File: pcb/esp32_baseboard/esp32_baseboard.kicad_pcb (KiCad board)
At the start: 2 copper layers, 220 x 160 mm, 49 parts, among them J1 Screw_12V_IN, J10 END_HOME2, J12 END_HOME3, J14 BUP_30S, J15 BUZZER_5V, J16 AOD4184, J17 TFT_LCD, J18 EC11_ENC, J23 TFT_TP, J24 595_CTRL, J25 595_Q, J5 28BYJ48, J6 28BYJ48, J7 28BYJ48, J8 END_HOME1, U1 ESP32_S3_DevKitC_1, U2 MP1584_5V3A, U3 TMC2209, U41 PC817, U42 PC817, U43 PC817, U44 PC817, U5 ULN2003AN, U6 ULN2003AN, U7 ULN2003AN

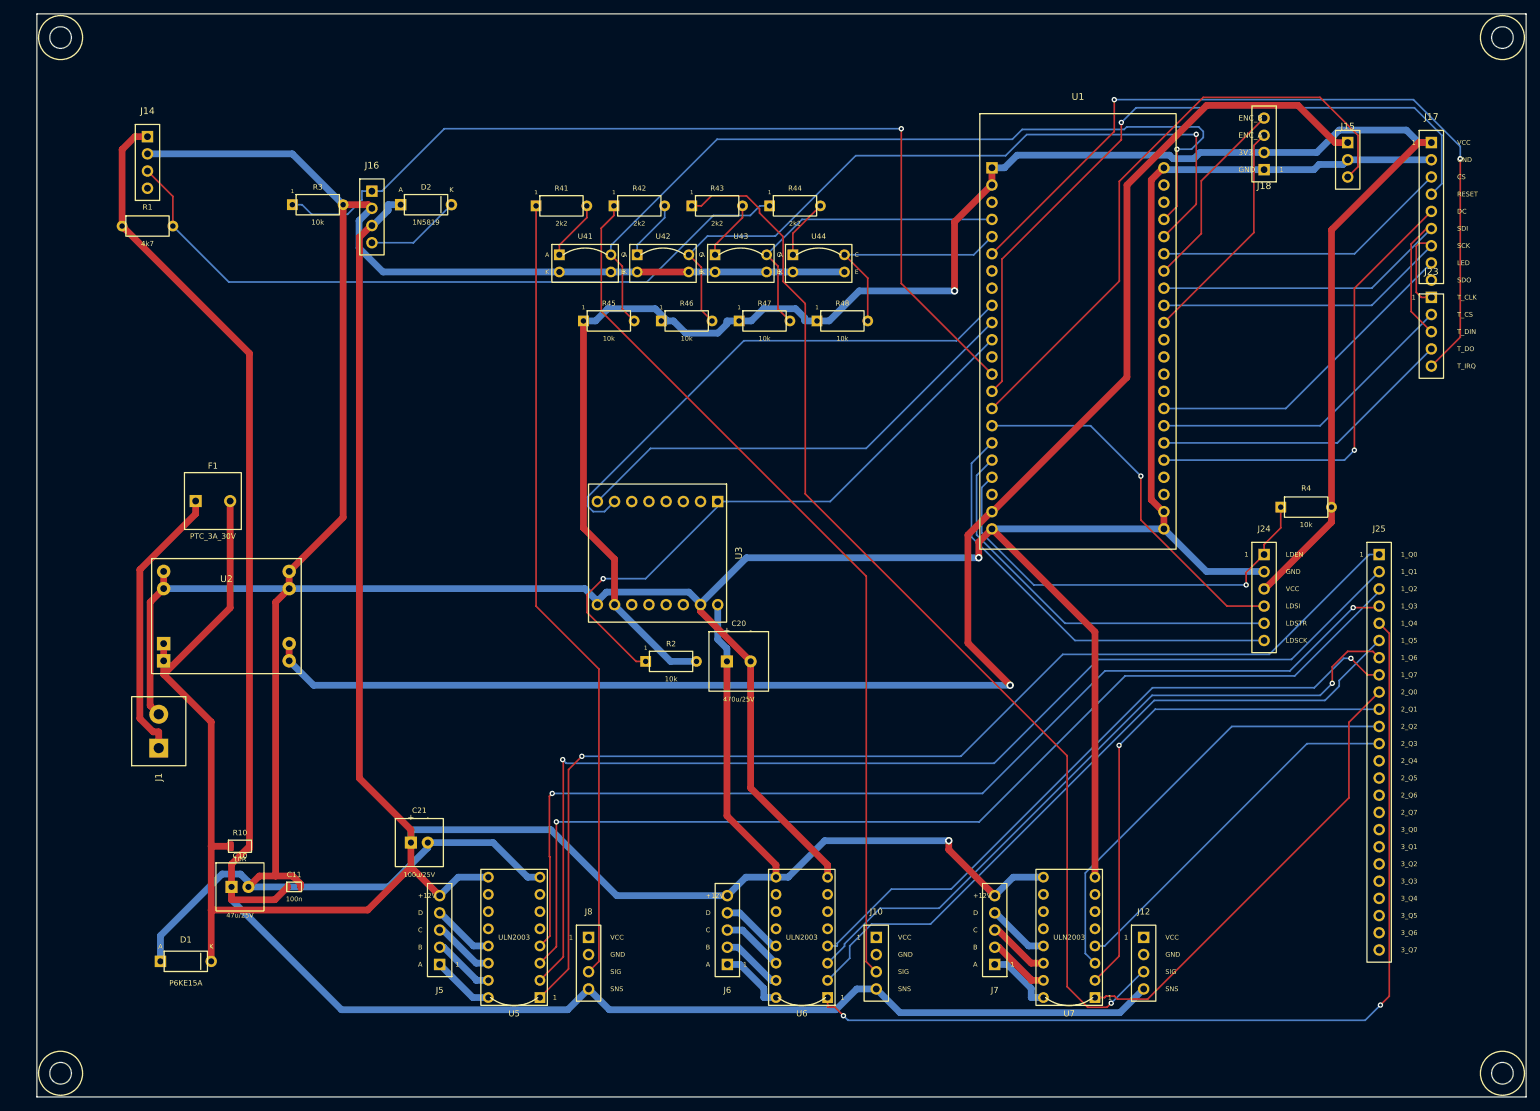
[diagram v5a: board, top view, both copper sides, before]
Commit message: update PCB cho phần power và opto và sắp xếp linh kiện
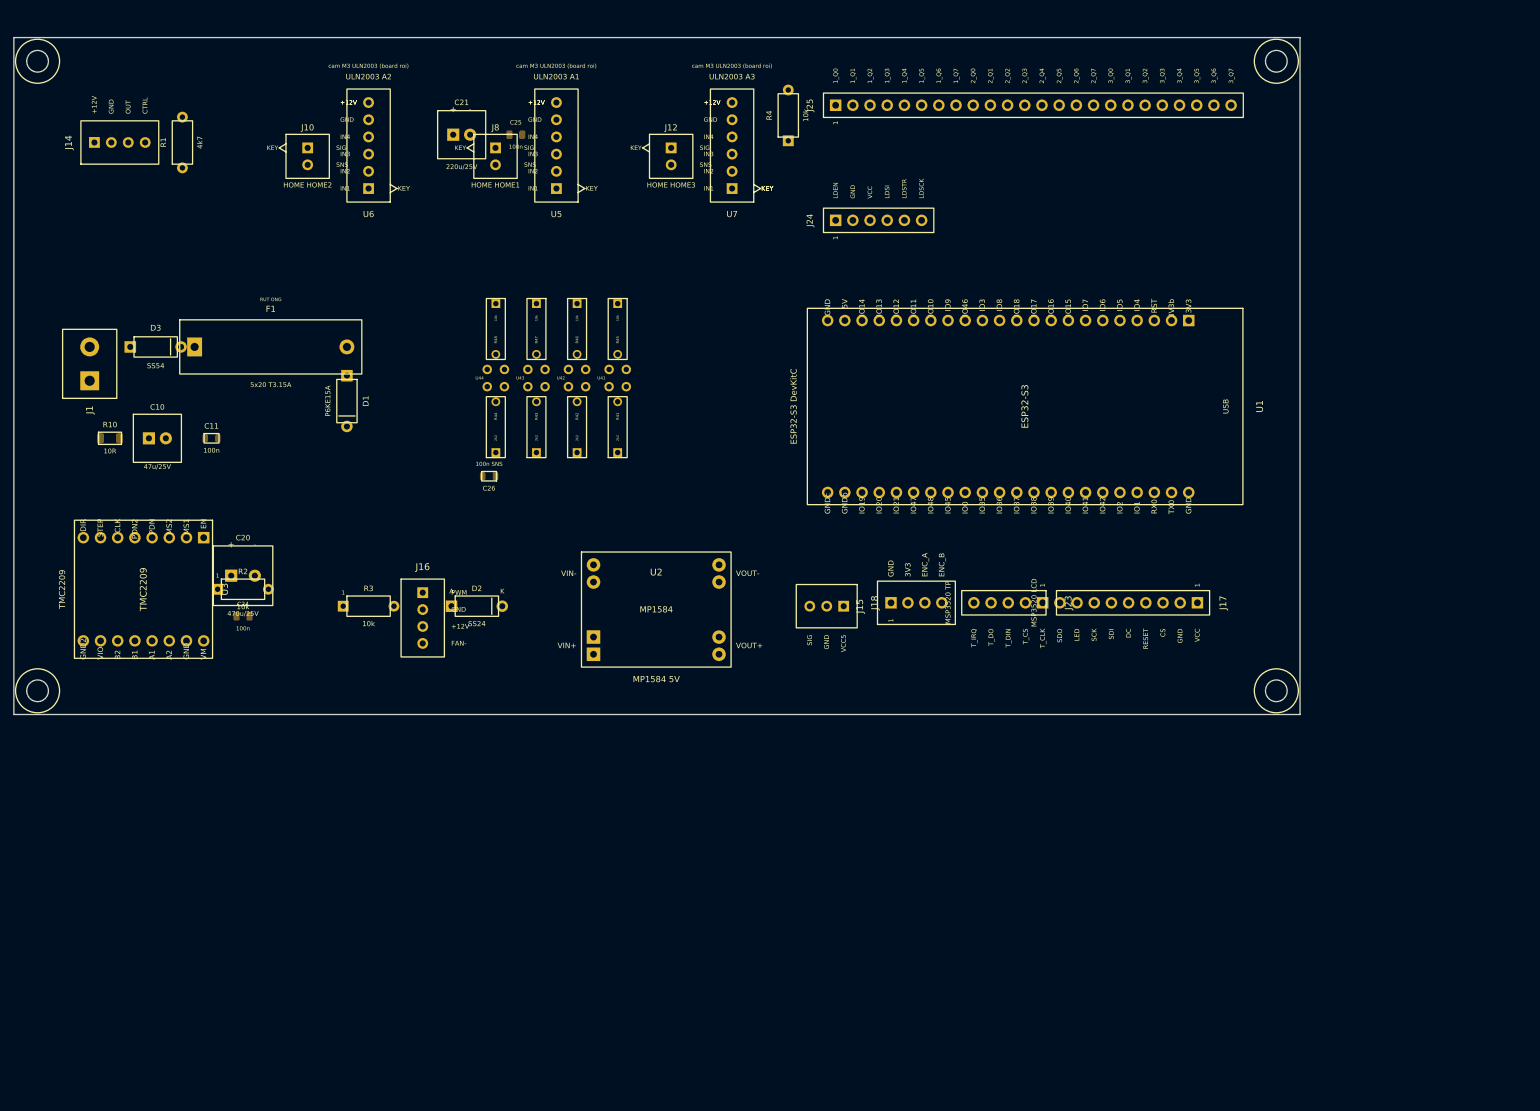
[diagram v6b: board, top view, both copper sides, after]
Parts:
- removed J5, J6, J7: 28BYJ48, ESP32_Carrier:PinHeader_1x05_BYJ
- added C24: 100n, ESP32_Carrier:C_0805_100n, F.Cu at (65.5, 119.0)
- added C25: 100n, ESP32_Carrier:C_0805_100n, F.Cu at (105.8, 47.9)
- added C26: 100n SNS, ESP32_Carrier:C_0805_100n, F.Cu at (101.8, 98.3)
- added D3: SS54, ESP32_Carrier:Diode_TVS_DO41, F.Cu at (52.5, 79.2)
- C21: value 100u/25V -> 220u/25V
- D2: value 1N5819 -> SS24
- F1: value PTC_3A_30V -> 5x20 T3.15A; footprint ESP32_Carrier:Fuse_PTC_Radial_5.1mm -> ESP32_Carrier:Fuse_Holder_5x20_Open
- J10: value END_HOME2 -> HOME HOME2; footprint ESP32_Carrier:PinHeader_1x04_Endstop -> ESP32_Carrier:JST_XH_02_Socket
- J12: value END_HOME3 -> HOME HOME3; footprint ESP32_Carrier:PinHeader_1x04_Endstop -> ESP32_Carrier:JST_XH_02_Socket
- J14: value BUP_30S -> BUP-30S; footprint ESP32_Carrier:PinHeader_1x04_BUP30S -> ESP32_Carrier:JST_XH_04_Socket
- J15: value BUZZER_5V -> BUZZER 5V; footprint ESP32_Carrier:PinHeader_1x03_Buzzer -> ESP32_Carrier:JST_XH_03_Socket
- J16: value AOD4184 -> AOD4184 12V; footprint ESP32_Carrier:PinHeader_1x04_MOSFET -> ESP32_Carrier:JST_XH_04_Socket
- J17: value TFT_LCD -> MSP3520 LCD
- J18: value EC11_ENC -> EC11 ENC; footprint ESP32_Carrier:PinHeader_1x04_ENC -> ESP32_Carrier:JST_XH_04_Socket
- J23: value TFT_TP -> MSP3520 TP
- J8: value END_HOME1 -> HOME HOME1; footprint ESP32_Carrier:PinHeader_1x04_Endstop -> ESP32_Carrier:JST_XH_02_Socket
- U1: value ESP32_S3_DevKitC_1 -> ESP32-S3 DevKitC
- U2: value MP1584_5V3A -> MP1584 5V
- U5: value ULN2003AN -> ULN2003 A1; footprint ESP32_Carrier:ULN2003AN -> ESP32_Carrier:ULN2003_Module
- U6: value ULN2003AN -> ULN2003 A2; footprint ESP32_Carrier:ULN2003AN -> ESP32_Carrier:ULN2003_Module
- U7: value ULN2003AN -> ULN2003 A3; footprint ESP32_Carrier:ULN2003AN -> ESP32_Carrier:ULN2003_Module
- moved J10 143.7 mm to (75.0, 49.8)
- moved J12 135.9 mm to (128.7, 49.8)
- moved U6 127.8 mm to (84.0, 55.8)
- moved U7 121.3 mm to (137.7, 55.8)
- moved J8 117.4 mm to (102.8, 49.8)
- moved U5 110.8 mm to (111.8, 55.8)
- moved C21 104.8 mm to (97.8, 47.9)
- moved J25 104.2 mm to (153.0, 43.5), turned to 90 degrees
- moved J15 101.2 mm to (154.2, 117.5), turned to -90 degrees
- moved R4 95.9 mm to (146.0, 45.0), turned to 90 degrees
- moved D1 86.1 mm to (80.8, 87.2), turned to -90 degrees
- moved J18 84.4 mm to (161.2, 117.0), turned to 90 degrees
- moved J24 80.3 mm to (153.0, 60.5), turned to 90 degrees
- moved J17 76.3 mm to (206.4, 117.0), turned to -90 degrees
- moved U3 76.1 mm to (50.8, 115.0)
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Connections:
- F1 pad 1: +12V_RAW -> +12V_PRE
- J10 pad 1: unconnected-(J10-VCC-Pad1) -> OPTO_IN2
- J10 pad 2: unconnected-(J10-GND-Pad2) -> +12V_SNS
- J12 pad 1: unconnected-(J12-VCC-Pad1) -> OPTO_IN3
- J12 pad 2: unconnected-(J12-GND-Pad2) -> +12V_SNS
- J8 pad 1: unconnected-(J8-VCC-Pad1) -> OPTO_IN1
- J8 pad 2: unconnected-(J8-GND-Pad2) -> +12V_SNS
- U5 pad 5: unconnected-(U5-IN5-Pad5) -> GND
- U5 pad 6: unconnected-(U5-IN6-Pad6) -> +12V
- U6 pad 5: unconnected-(U6-IN5-Pad5) -> GND
- U6 pad 6: unconnected-(U6-IN6-Pad6) -> +12V
- U7 pad 5: unconnected-(U7-IN5-Pad5) -> GND
- U7 pad 6: unconnected-(U7-IN6-Pad6) -> +12V
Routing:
- net GND: track 696.4 -> 0.00 mm, vias 1 -> 0
- net +12V: track 385.4 -> 0.00 mm, vias 1 -> 0
- net +3V3: track 288.3 -> 0.00 mm, vias 1 -> 0
- net +12V_SNS: track 283.4 -> 0.00 mm
- net +5V: track 236.6 -> 0.00 mm, vias 1 -> 0
- net SR_Q0: track 168.3 -> 0.00 mm, vias 1 -> 0
- net SR_Q1: track 166.6 -> 0.00 mm, vias 1 -> 0
- net OPTO_IN3: track 159.9 -> 0.00 mm, vias 1 -> 0
- net SR_Q2: track 157.9 -> 0.00 mm, vias 1 -> 0
- net SR_Q3: track 157.0 -> 0.00 mm, vias 2 -> 0
- net SR_Q4: track 142.4 -> 0.00 mm, vias 2 -> 0
- net BLOWER: track 138.3 -> 0.00 mm, vias 1 -> 0
- net OPTO_IN2: track 130.7 -> 0.00 mm
- net OPTO_OUT1: track 124.3 -> 0.00 mm, vias 1 -> 0
- net T_IRQ: track 118.5 -> 0.00 mm, vias 2 -> 0
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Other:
- board size 220 x 160 mm -> 190 x 100 mm
- board text removed: "+12V VIA 3A"
- board text removed: "1: POWER J1+F1+D1+U2+RC"
- board text removed: "2: MCU U1 ESP32-S3 DevKitC"
- board text removed: "3: TMC U3 + Mot pins (NEMA17 on module)"
- board text removed: "4: OPTO U41-U44 PC817 + R2k2/10k"
- board text removed: "5: SHIFT U10 595-24IO + J24/J25 + R4"
- board text removed: "A1: HOME1+U5+J5"
- board text removed: "A2: HOME2+U6+J6"
- board text removed: "A3: HOME3+U7+J7"
- board text removed: "All parts TOP (F.Cu); B.Cu = routing only. Eco1 cluster = cyan"
- board text removed: "B: BLOWER J16 AOD4184 + R3/D2"
- board text removed: "Brn +12 Blu GND Blk OUT Wht CTRL"
- board text removed: "C20 470u/25V TMC"
- board text removed: "C21 100u/25V ULN"
- board text removed: "C: HMI J17 LCD + J23 TP + J18 ENC + J15 BZ"
- board text removed: "D2 K(band)->+12V"
- board text removed: "F1 PTC + D1 TVS"
- board text removed: "GND 3V3 A=IO38 B=IO41"
- board text removed: "GND star gap chi gap tai J1-"
- board text removed: "J10 HOME2"
- board text removed: "J12 HOME3"
- board text removed: "J14 BUP-30S NPN"
- board text removed: "J16 AOD4184 +12V pump"
- board text removed: "J18 ENC wall-mount EC11"
- board text removed: "J5 28BYJ BYJ1"
- board text removed: "J6 28BYJ BYJ2"
- board text removed: "J7 28BYJ BYJ3"
- board text removed: "J8 HOME1"
- board text removed: "LCD"
- board text removed: "M3x4 corner mount"
- board text removed: "OPTO PC817x8 + 2k2/10k"
- board text removed: "R1 4k7 pullup NPN"
- board text removed: "R2 EN_TMC pull-up 10k"
- board text removed: "R3 BLOWER pull-down 10k"
- board text removed: "R4 LDEN/OE pull-up 10k"
- board text removed: "R41 LED HOME1"
- board text removed: "R42 LED HOME2"
- board text removed: "R43 LED HOME3"
- board text removed: "R44 LED BUP"
- board text removed: "R45 PU HOME1"
- board text removed: "R46 PU HOME2"
- board text removed: "R47 PU HOME3"
- board text removed: "R48 PU BUP"
- board text removed: "RC SNS FILTER"
- board text removed: "STAR +12V: MOT 2.5mm | SNS 0.5mm+RC"
- board text removed: "Shopee thegioimodule 3x595"
- board text removed: "TP"
- board text removed: "U10 74HC595-24IO module"
- board text removed: "U: BUP-30S J14 + R1 4k7"
